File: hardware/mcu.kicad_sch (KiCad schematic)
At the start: 36 parts, among them J2 Conn_01x03_Socket, J3 Conn_01x03_Socket, SW1 SW_Push, U1 STM32F405RGT7, X1 8MHz

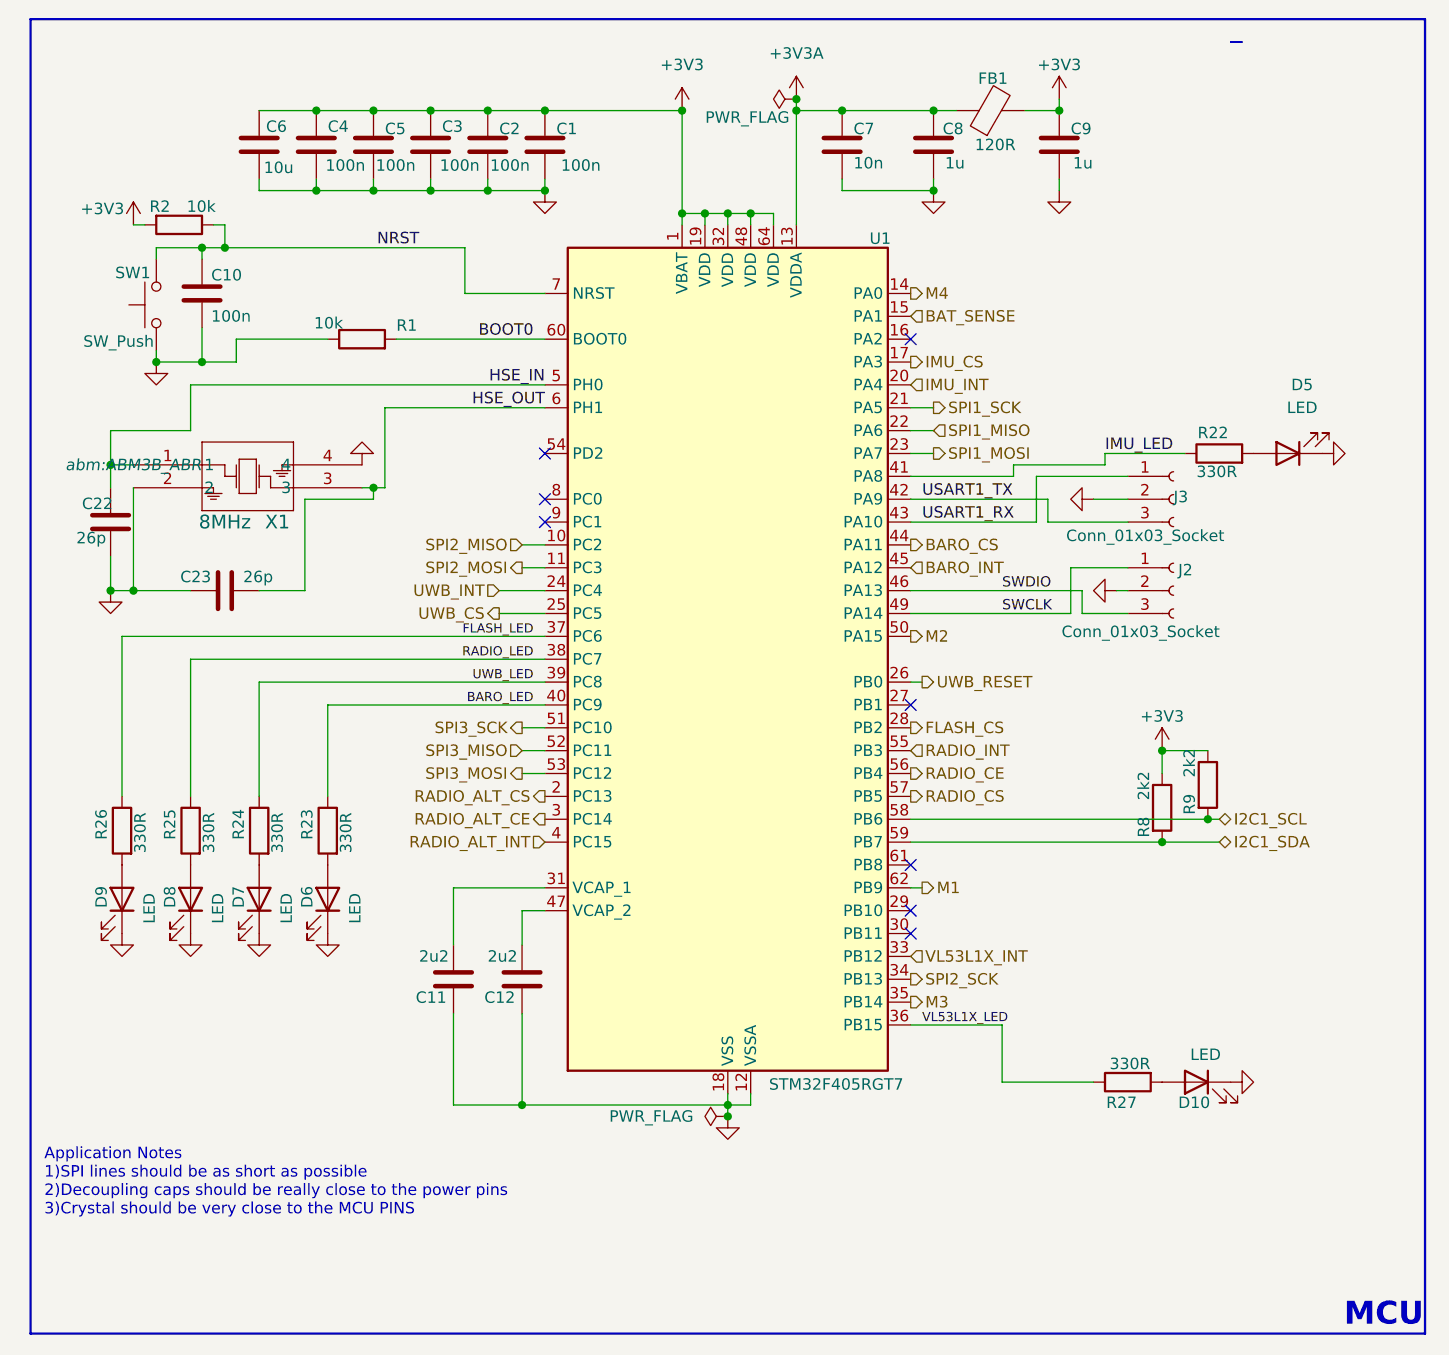
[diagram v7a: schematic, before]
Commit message: feat(kicad): Rerouted board and changed nets to provide ease in routing
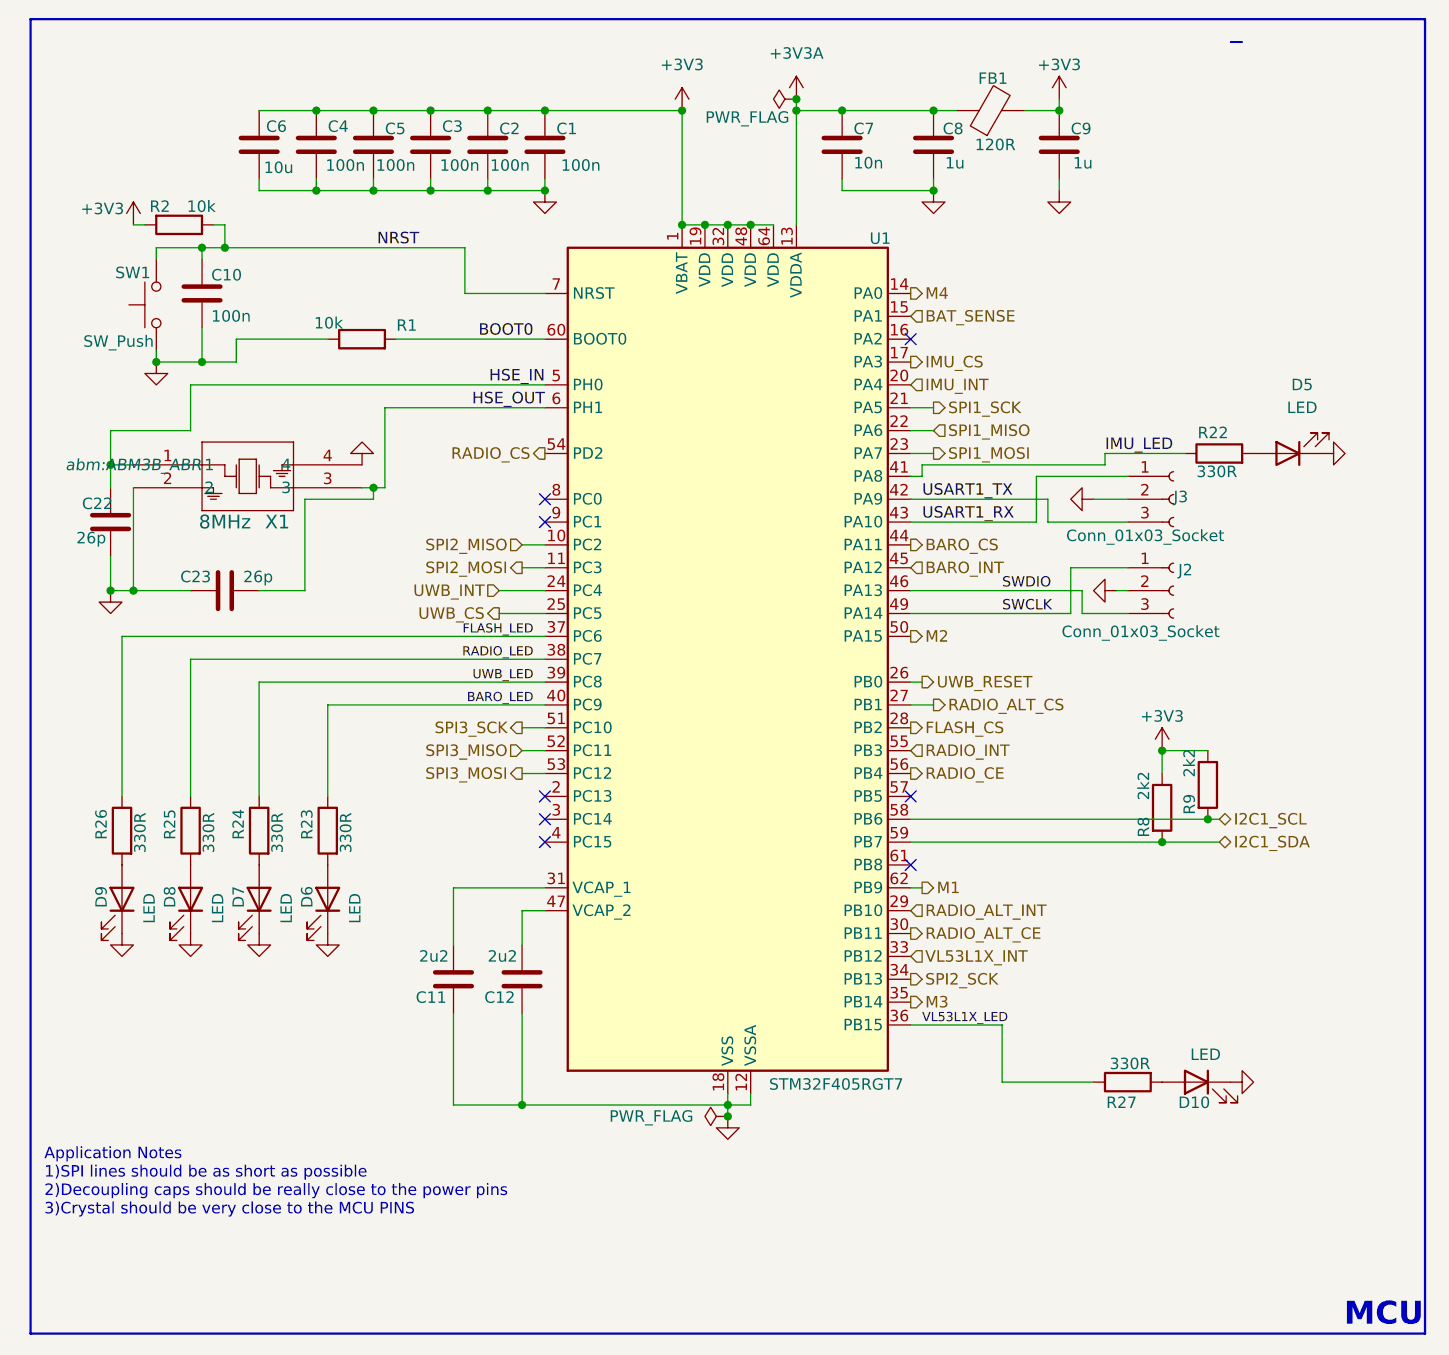
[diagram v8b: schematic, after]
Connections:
- net RADIO_ALT_CE: now also U1.30 (PB11); no longer U1.3 (PC14)
- net RADIO_ALT_CS: now also U1.27 (PB1); no longer U1.2 (PC13)
- net RADIO_ALT_INT: now also U1.29 (PB10); no longer U1.4 (PC15)
- net RADIO_CS: now also U1.54 (PD2); no longer U1.57 (PB5)
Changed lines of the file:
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@@
 	)
 	(junction
-		(at 149.86 39.37)
+		(at 147.32 40.64)
 		(diameter 0)
 		(color 0 0 0 0)
@@
 	)
 	(junction
-		(at 144.78 39.37)
-		(diameter 0)
-		(color 0 0 0 0)
-	)
-	(junction
-		(at 142.24 39.37)
+		(at 142.24 40.64)
 		(diameter 0)
 		(color 0 0 0 0)
@@
 	)
 	(junction
+		(at 144.78 40.64)
+		(diameter 0)
+		(color 0 0 0 0)
+	)
+	(junction
 		(at 184.15 27.94)
 		(diameter 0)
@@
 	)
 	(junction
-		(at 147.32 39.37)
-		(diameter 0)
-		(color 0 0 0 0)
-	)
-	(junction
 		(at 114.3 27.94)
 		(diameter 0)
@@
 	)
 	(junction
+		(at 149.86 40.64)
+		(diameter 0)
+		(color 0 0 0 0)
+	)
+	(junction
 		(at 127 36.83)
 		(diameter 0)
@@
 	)
 	(no_connect
-		(at 167.64 93.98)
-	)
-	(no_connect
-		(at 167.64 116.84)
+		(at 167.64 104.14)
 	)
 	(no_connect
@@
 	)
 	(no_connect
-		(at 167.64 119.38)
+		(at 127 106.68)
+	)
+	(no_connect
+		(at 127 109.22)
 	)
 	(no_connect
@@
 	)
 	(no_connect
-		(at 127 66.04)
-	)
-	(wire
-		(pts
-			(xy 152.4 39.37) (xy 152.4 40.64)
-		)
-		(stroke
-			(width 0)
-			(type default)
-		)
+		(at 127 104.14)
 	)
 	(wire
@@
 	(wire
 		(pts
+			(xy 168.91 68.58) (xy 167.64 68.58)
+		)
+		(stroke
+			(width 0)
+			(type default)
+		)
+	)
+	(wire
+		(pts
 			(xy 170.18 27.94) (xy 172.72 27.94)
 		)
@@
 	(wire
 		(pts
+			(xy 149.86 40.64) (xy 152.4 40.64)
+		)
+		(stroke
+			(width 0)
+			(type default)
+		)
+	)
+	(wire
+		(pts
 			(xy 154.94 27.94) (xy 154.94 40.64)
 		)
@@
 	(wire
 		(pts
-			(xy 144.78 39.37) (xy 144.78 40.64)
-		)
-		(stroke
-			(width 0)
-			(type default)
-		)
-	)
-	(wire
-		(pts
 			(xy 160.02 27.94) (xy 170.18 27.94)
 		)
@@
 	(wire
 		(pts
+			(xy 147.32 40.64) (xy 149.86 40.64)
+		)
+		(stroke
+			(width 0)
+			(type default)
+		)
+	)
+	(wire
+		(pts
 			(xy 87.63 63.5) (xy 78.74 63.5)
 		)
@@
 	(wire
 		(pts
-			(xy 149.86 39.37) (xy 149.86 40.64)
-		)
-		(stroke
-			(width 0)
-			(type default)
-		)
-	)
-	(wire
-		(pts
 			(xy 78.74 67.31) (xy 81.28 67.31)
 		)
@@
 	(wire
 		(pts
+			(xy 144.78 40.64) (xy 147.32 40.64)
+		)
+		(stroke
+			(width 0)
+			(type default)
+		)
+	)
+	(wire
+		(pts
 			(xy 107.95 71.12) (xy 107.95 69.85)
 		)
@@
 	(wire
 		(pts
-			(xy 147.32 39.37) (xy 147.32 40.64)
-		)
-		(stroke
-			(width 0)
-			(type default)
-		)
-	)
-	(wire
-		(pts
 			(xy 107.95 69.85) (xy 109.22 69.85)
 		)
@@
 	(wire
 		(pts
-			(xy 142.24 39.37) (xy 152.4 39.37)
+			(xy 142.24 40.64) (xy 144.78 40.64)
 		)
 		(stroke
@@
 	(wire
 		(pts
-			(xy 179.07 68.58) (xy 179.07 67.31)
-		)
-		(stroke
-			(width 0)
-			(type default)
-		)
-	)
-	(wire
-		(pts
 			(xy 167.64 73.66) (xy 181.61 73.66)
 		)
@@
 	(wire
 		(pts
-			(xy 142.24 39.37) (xy 142.24 40.64)
-		)
-		(stroke
-			(width 0)
-			(type default)
-		)
-	)
-	(wire
-		(pts
 			(xy 191.77 73.66) (xy 182.88 73.66)
 		)
@@
 	(wire
 		(pts
+			(xy 168.91 67.31) (xy 168.91 68.58)
+		)
+		(stroke
+			(width 0)
+			(type default)
+		)
+	)
+	(wire
+		(pts
 			(xy 78.74 81.28) (xy 81.28 81.28)
 		)
@@
 	(wire
 		(pts
-			(xy 167.64 68.58) (xy 179.07 68.58)
+			(xy 168.91 67.31) (xy 189.23 67.31)
 		)
 		(stroke
@@
 	(wire
 		(pts
-			(xy 179.07 67.31) (xy 189.23 67.31)
+			(xy 170.18 93.98) (xy 167.64 93.98)
 		)
 		(stroke
@@
 	(wire
 		(pts
-			(xy 142.24 27.94) (xy 142.24 39.37)
+			(xy 142.24 27.94) (xy 142.24 40.64)
 		)
 		(stroke
@@
 		)
 	)
-	(hierarchical_label "RADIO_ALT_CE"
-		(shape output)
-		(at 127 106.68 180)
-		(effects
-			(font
-				(size 1.27 1.27)
-			)
-			(justify right)
-		)
-	)
 	(hierarchical_label "IMU_CS"
 		(shape output)
@@
 		)
 	)
+	(hierarchical_label "RADIO_ALT_CE"
+		(shape output)
+		(at 167.64 119.38 0)
+		(effects
+			(font
+				(size 1.27 1.27)
+			)
+			(justify left)
+		)
+	)
 	(hierarchical_label "SPI1_MISO"
 		(shape input)
@@
 		)
 	)
-	(hierarchical_label "RADIO_ALT_CS"
-		(shape output)
-		(at 127 104.14 180)
-		(effects
-			(font
-				(size 1.27 1.27)
-			)
-			(justify right)
-		)
-	)
-	(hierarchical_label "RADIO_ALT_INT"
-		(shape input)
-		(at 127 109.22 180)
-		(effects
-			(font
-				(size 1.27 1.27)
-			)
-			(justify right)
-		)
-	)
 	(hierarchical_label "FLASH_CS"
 		(shape output)
@@
 		)
 	)
+	(hierarchical_label "RADIO_ALT_CS"
+		(shape output)
+		(at 170.18 93.98 0)
+		(effects
+			(font
+				(size 1.27 1.27)
+			)
+			(justify left)
+		)
+	)
 	(hierarchical_label "UWB_CS"
 		(shape output)
@@
 		)
 	)
+	(hierarchical_label "RADIO_ALT_INT"
+		(shape input)
+		(at 167.64 116.84 0)
+		(effects
+			(font
+				(size 1.27 1.27)
+			)
+			(justify left)
+		)
+	)
 	(hierarchical_label "M4"
 		(shape output)
@@
 		)
 	)
-	(hierarchical_label "RADIO_CS"
-		(shape output)
-		(at 167.64 104.14 0)
-		(effects
-			(font
-				(size 1.27 1.27)
-			)
-			(justify left)
-		)
-	)
 	(hierarchical_label "VL53L1X_INT"
 		(shape input)
@@
 		)
 	)
+	(hierarchical_label "RADIO_CS"
+		(shape output)
+		(at 127 66.04 180)
+		(effects
+			(font
+				(size 1.27 1.27)
+			)
+			(justify right)
+		)
+	)
